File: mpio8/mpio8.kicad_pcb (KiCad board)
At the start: 2 copper layers, 63.5 x 81.3 mm, 80 parts, among them J1 Conn_01x02_Male, J10 Conn_01x04_Male, J11 Conn_01x04_Male, J2 JST PHR4 (STEMMA), J3 Conn_02x05_Odd_Even, J4 Conn_01x02_Male, J5 Conn_01x02_Male, J6 Conn_01x02_Male, J7 Conn_01x02_Male, J8 Conn_01x04_Male, J9 Conn_01x04_Male, K1 J102-1C, K2 J102-1C, K3 J102-1C, K4 J102-1C, Q1 IRLZ44N, Q10 MMBT3904, Q2 MMBT3904, Q3 IRLZ44N, Q4 MMBT3904, Q5 IRLZ44N, Q6 MMBT3904, Q7 IRLZ44N, Q8 MMBT3904, Q9 MMBT3904, U1 TCA9554DW, U2 MIC4427, U3 MIC4427, U4 PC817, U5 PC817, U6 PC817, U7 PC817

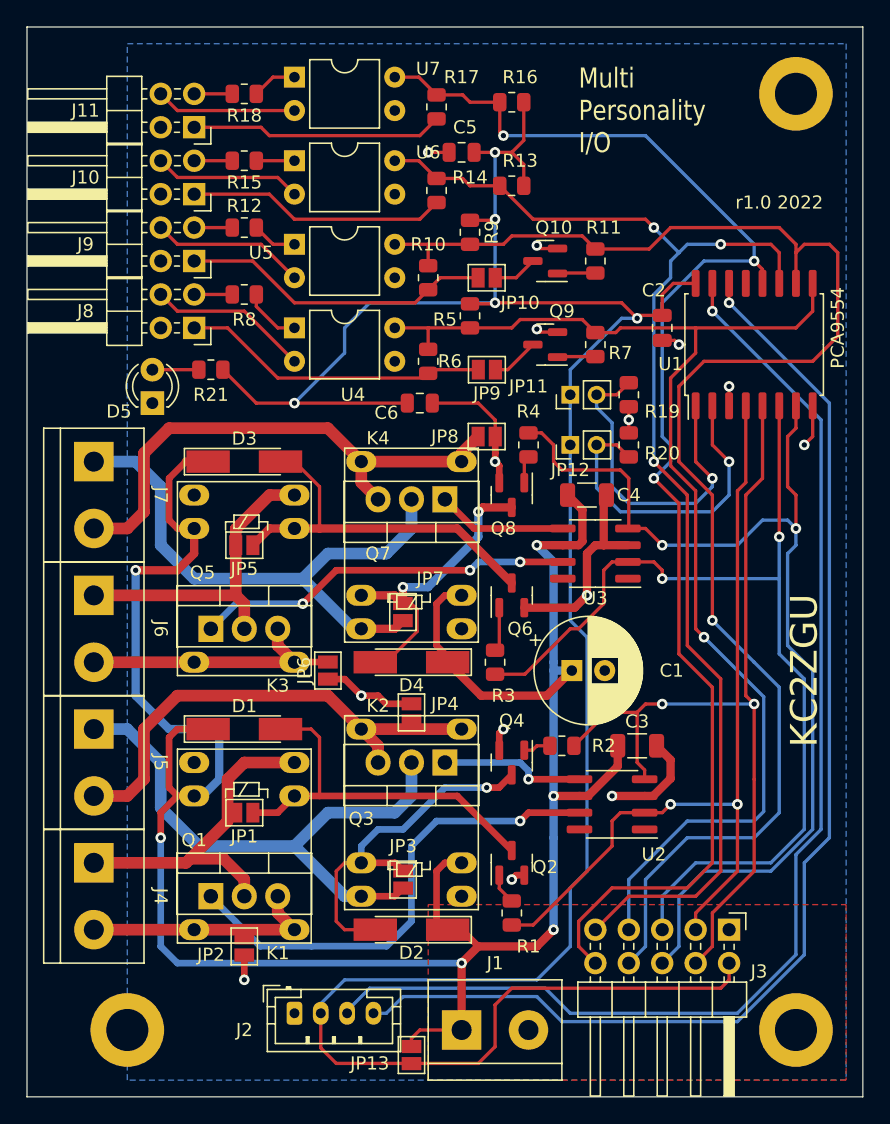
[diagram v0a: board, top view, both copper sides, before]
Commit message: mpio8: r1.1
 - fix I2C connector pinout
 - DIP switch for address pins
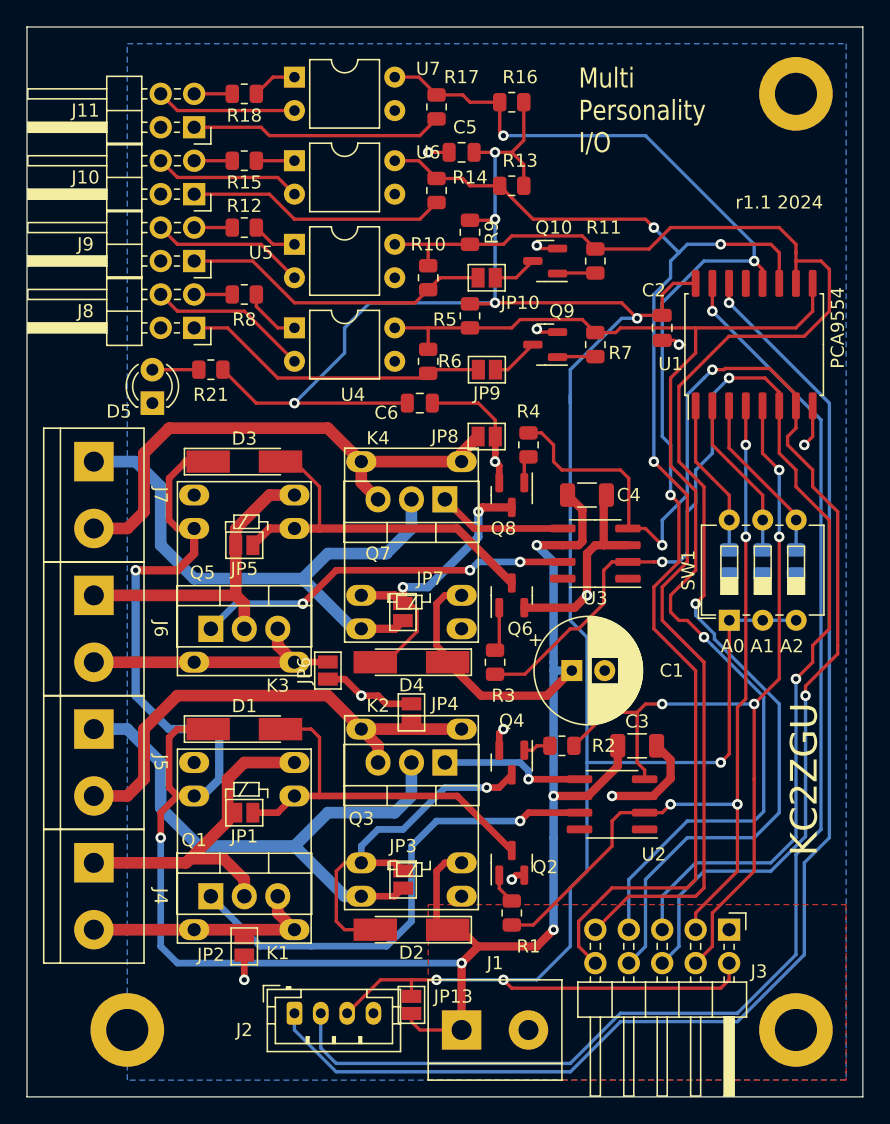
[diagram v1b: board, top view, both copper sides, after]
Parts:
- removed JP11, JP12: Jumper_2_Open, Connector_PinHeader_2.00mm:PinHeader_1x02_P2.00mm_Vertical
- added R22: 10K, Resistor_SMD:R_0805_2012Metric, B.Cu at (134.6, 96.5)
- added SW1: SW_DIP_x03, Button_Switch_THT:SW_DIP_SPSTx03_Slide_6.7x9.18mm_W7.62mm_P2.54mm_LowProfile, F.Cu at (129.6, 101.0)
- R19, R20: moved to B.Cu
- moved R19 14.8 mm to (129.5, 96.5)
- moved R20 13.5 mm to (132.1, 96.5), turned to 90 degrees
- moved JP13 3.81 mm to (105.4, 130.2), turned to 90 degrees
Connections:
- J2 pad 1: GND -> /SCL
- J2 pad 2: VCC -> /SDA
- J2 pad 3: /SDA -> VCC
- J2 pad 4: /SCL -> GND
- U1 pad 3: GND -> Net-(U1-A2)
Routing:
- net IO2: track 75.9 -> 89.8 mm, vias 2 -> 3
- net Net-(U1-A0): track 25.6 -> 12.0 mm, vias 1 -> 0
- net Net-(U1-A2): track 0.00 -> 13.1 mm
- net IO3: track 79.6 -> 92.4 mm, vias 2 -> 3
- net Net-(U1-A1): track 24.7 -> 12.5 mm, vias 1 -> 0
- net /SCL: track 91.1 -> 100.0 mm
- net /SDA: track 92.8 -> 98.1 mm
- net VCC: track 191.2 -> 195.6 mm, vias 5 -> 8
- net GND: track 58.6 -> 55.1 mm, vias 14 -> 12
- net IO5: track 115.1 -> 111.7 mm
- net IO4: track 93.2 -> 95.2 mm
- net IO7: track 106.3 -> 105.8 mm
- net IO6: track 96.2 -> 96.7 mm
- net IO1: track 65.3 -> 65.8 mm, vias 2 -> 4
- net IO0: vias 2 -> 4
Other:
- board text added: "A0 A1 A2"
- board text added: "KC2ZGU 2024"
- board text added: "r1.1 2024"
- board text removed: "I2C Addr: A0=JP11 A1=JP12 A2=0"
- board text removed: "KC2ZGU 2022"
- board text removed: "r1.0 2022"
